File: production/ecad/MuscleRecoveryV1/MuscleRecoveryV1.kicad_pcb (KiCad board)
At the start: 4 copper layers, 115.2 x 70.5 mm, 130 parts, among them IC1 LC709203FQH-01TWG, J1 AudioJack3, J2 Screw_Terminal_01x03, J3 Motor_Screw_Terminal, J4 USB_C_Receptacle_USB2.0, J5 Screw_Terminal_01x10, J6 Screw_Terminal_01x06, J7 Conn_01x11_Pin, Q1 FDN340P, Q2 AO3400A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

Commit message: pushing current layout and other changes to be able to pull
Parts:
- removed J4: USB_C_Receptacle_USB2.0, Connector_USB:USB_C_Plug_Molex_105444
- added J8: Screw_Terminal_01x07, Connector_PinHeader_2.54mm:PinHeader_1x07_P2.54mm_Vertical, F.Cu at (117.9, 173.6)
- added J9: Screw_Terminal_01x02, Connector_PinHeader_2.54mm:PinHeader_1x02_P2.54mm_Vertical, F.Cu at (218.2, 83.4)
- J5: value Screw_Terminal_01x10 -> USB4110-GF-A; footprint Connector_PinHeader_2.54mm:PinHeader_1x10_P2.54mm_Vertical -> Muscle_Recovery_Footprint_Library:USB4110-GF-A_GCT
- R63: value 0 -> DNP
- moved R24 156.8 mm to (102.9, 165.9), turned to 90 degrees
- moved R46 155.6 mm to (107.7, 162.6)
- moved R4 154.6 mm to (99.9, 156.5)
- moved R63 154.4 mm to (113.8, 161.2), turned to 180 degrees
- moved R23 154.4 mm to (102.8, 151.1)
- moved R7 153.3 mm to (99.8, 158.8)
- moved C3 152.8 mm to (99.7, 162.6), turned to 180 degrees
- moved R45 152.5 mm to (108.0, 144.0)
- moved R22 151.0 mm to (106.8, 151.1)
- moved R6 150.9 mm to (103.7, 162.6), turned to 180 degrees
- moved R5 150.3 mm to (103.7, 156.5)
- moved R64 149.9 mm to (117.7, 161.2)
- moved R28 149.7 mm to (117.7, 164.0)
- moved R19 149.6 mm to (110.1, 150.4), turned to 90 degrees
- moved C4 146.6 mm to (104.4, 159.5), turned to 90 degrees
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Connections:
- C16 pad 1: +3.3V -> +3V3
- C8 pad 1: +3.3V -> +3V3
- C9 pad 1: +3.3V -> +3V3
- D7 pad 1: +3.3V -> +3V3
- J1 pad 1: (no net) -> RA
- J1 pad 2: (no net) -> RL
- J1 pad 3: (no net) -> LA
- J3 pad 1: +3.3V -> +3V3
- J6 pad 2: IO35 -> IO17
- J7 pad 2: +3.3V -> +3V3
- R10 pad 1: Net-(J4-CC1) -> Net-(J5-CC1)
- R11 pad 1: +3.3V -> +3V3
- R12 pad 1: +3.3V -> +3V3
- R16 pad 1: +3.3V -> +3V3
- R36 pad 1: +BATT -> +3V3
- R9 pad 1: Net-(J4-CC2) -> Net-(J5-CC2)
- S1 pad 4: +3.3V -> +3V3
- S4 pad 4: +3.3V -> +3V3
- SCL1 pad 1: SDA -> SCL
- TFT_CLK1 pad 1: TFT_CLK -> SCK
- U1 pad 2: +3.3V -> +3V3
- U3 pad 6: +3.3V -> +3V3
- U3 pad 7: +3.3V -> +3V3
- U6 pad 28: unconnected-(U6-IO17-Pad28) -> IO17
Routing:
- net IO26: track 0.00 -> 19.6 mm
- net IO27: track 0.00 -> 14.7 mm
- net IO32: track 0.00 -> 13.7 mm
- added copper zone on In1.Cu, net GND

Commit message: saving changes
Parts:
- moved J8 62.9 mm to (118.1, 110.8), turned to 0 degrees
- moved R24 60.7 mm to (125.2, 109.5), turned to 0 degrees
- moved C3 60.6 mm to (128.8, 109.5), turned to 0 degrees
- moved R7 59.4 mm to (131.8, 108.8), turned to -90 degrees
- moved R4 59.0 mm to (134.8, 108.9), turned to -90 degrees
- moved IO0 57.9 mm to (176.3, 109.8)
- moved TP4 56.8 mm to (178.3, 127.9)
- moved R6 56.4 mm to (128.8, 112.1), turned to 0 degrees
- moved D5 55.8 mm to (123.2, 112.7)
- moved R23 55.1 mm to (138.4, 109.0), turned to -90 degrees
- moved C4 54.2 mm to (131.8, 112.7)
- moved R5 53.8 mm to (134.8, 112.6), turned to -90 degrees
- moved R46 52.6 mm to (128.8, 114.5), turned to 180 degrees
- moved R62 50.8 mm to (152.3, 101.3), turned to -90 degrees
- moved C10 50.8 mm to (141.9, 111.9)
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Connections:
- J6 pad 2: IO17 -> IO32
- J6 pad 3: IO32 -> IO17
- J6 pad 4: IO27 -> IO26
- J6 pad 5: IO26 -> IO27
- J8 pad 3: LOD+ -> LOD-
- J8 pad 4: LOD- -> LOD+
- J8 pad 5: REF -> SDN
- J8 pad 7: SDN -> REF
- R44 pad 1: Net-(U5-FR) -> SW
- R44 pad 2: SW -> Net-(U5-FR)
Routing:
- net IO26: track 19.6 -> 0.00 mm
- net IO27: track 14.7 -> 0.00 mm
- net IO32: track 13.7 -> 0.00 mm
- net +3V3: track 6.19 -> 0.00 mm
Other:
- board size 115.2 x 70.5 mm -> 92.6 x 67.3 mm

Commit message: my first complete pcb draft
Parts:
- moved GND1 17.0 mm to (162.5, 129.2)
- moved 3v31 14.0 mm to (166.5, 129.2)
- moved SCL1 9.33 mm to (178.8, 81.9)
- moved SDA1 3.45 mm to (177.7, 75.1)
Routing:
- net GND: track 0.00 -> 101.9 mm, vias 0 -> 43
- net SDA: track 0.00 -> 99.5 mm, vias 0 -> 2
- net SCK: track 0.00 -> 91.6 mm, vias 0 -> 2
- net +3V3: track 0.00 -> 88.5 mm, vias 0 -> 25
- net EN: track 0.00 -> 86.1 mm, vias 0 -> 2
- net TFT_RST: track 0.00 -> 77.8 mm, vias 0 -> 2
- net MISO: track 0.00 -> 76.4 mm, vias 0 -> 2
- net SCL: track 0.00 -> 68.8 mm
- net MOSI: track 0.00 -> 66.8 mm, vias 0 -> 2
- net REF: track 0.00 -> 63.5 mm, vias 0 -> 2
- net IO0: track 0.00 -> 56.1 mm
- net LIT: track 0.00 -> 54.4 mm
- net TFT_DC: track 0.00 -> 53.0 mm, vias 0 -> 2
- net RXD0: track 0.00 -> 49.9 mm, vias 0 -> 2
- net Vout: track 0.00 -> 49.9 mm
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- added copper zone on In2.Cu, net +3V3
- added copper zone on In2.Cu, net +BATT
- added copper zone on In2.Cu, net VBUS

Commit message: final pcb updates
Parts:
- moved C8 12.9 mm to (193.3, 111.9), turned to 90 degrees
- moved C17 11.9 mm to (203.2, 83.1), turned to 90 degrees
- moved C9 10.8 mm to (195.5, 111.9), turned to 90 degrees
- moved SDA1 8.44 mm to (185.5, 78.3)
- moved SCL1 7.97 mm to (176.9, 74.2)
- moved D2 3.89 mm to (186.6, 99.6), turned to 0 degrees
- moved C15 2.67 mm to (186.1, 97.2), turned to 0 degrees
- moved R31 2.22 mm to (177.9, 76.7), turned to 0 degrees
- moved C5 2.19 mm to (204.1, 98.0), turned to 0 degrees
- moved R30 2.08 mm to (177.9, 79.5)
- moved TFT_CLK1 1.68 mm to (127.6, 102.9)
- moved R51 1.34 mm to (121.7, 94.4)
- moved R50 1.29 mm to (121.7, 97.2)
- moved R52 1.28 mm to (121.7, 91.6)
- moved R56 1.26 mm to (121.7, 81.0)
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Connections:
- C17 pad 1: +BATT -> GND
- C17 pad 2: GND -> +BATT
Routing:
- net SDA: track 99.5 -> 78.7 mm
- net IO0: track 56.1 -> 38.7 mm, vias 0 -> 2
- net GND: track 101.9 -> 88.7 mm, vias 43 -> 40
- net RTS: track 21.4 -> 10.1 mm
- net USB-: track 10.4 -> 20.6 mm, vias 0 -> 2
- net SCL: track 68.8 -> 78.9 mm, vias 0 -> 2
- net USB+: track 13.3 -> 20.6 mm
- net +3V3: track 88.5 -> 82.8 mm, vias 25 -> 24
- net VBUS: track 30.9 -> 25.8 mm
- net +BATT: track 21.9 -> 18.0 mm, vias 4 -> 3
- net TFT_RST: track 77.8 -> 81.5 mm
- net DTR: track 23.4 -> 20.0 mm
- net Net-(D2-K): track 8.14 -> 5.03 mm
- net Net-(U3-~{RST}): track 3.44 -> 0.50 mm
- net SCK: track 91.6 -> 94.2 mm
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- added copper zone on F.Cu, net +3V3

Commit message: extra save
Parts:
- moved R15 13.4 mm to (192.3, 120.3), turned to 180 degrees
- moved R13 12.6 mm to (192.3, 113.7), turned to 0 degrees
- moved R14 12.6 mm to (192.3, 116.0), turned to 180 degrees
- moved R16 12.0 mm to (192.3, 118.3), turned to 0 degrees
- moved R17 11.6 mm to (203.6, 115.8), turned to 0 degrees
- moved R18 11.4 mm to (203.6, 117.9), turned to 0 degrees
- moved R40 4.34 mm to (185.5, 121.4), turned to 90 degrees
- moved SD_CS1 3.85 mm to (124.8, 83.8)
- moved TFT_CLK1 3.84 mm to (124.9, 100.2)
- moved TFT_DC1 3.37 mm to (124.8, 86.4)
- moved MOSI1 3.33 mm to (124.9, 94.5)
- moved TFT_CS1 3.19 mm to (124.8, 91.7)
- moved MISO1 3.08 mm to (124.9, 97.2)
- moved TFT_RST1 2.96 mm to (124.8, 89.0)
- moved R57 1.75 mm to (143.6, 83.6)
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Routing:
- net GND: track 88.7 -> 129.9 mm, vias 40 -> 45
- net DTR: track 20.0 -> 39.1 mm, vias 0 -> 2
- net TXD0: track 48.1 -> 65.8 mm
- net RXD0: track 49.9 -> 63.3 mm
- net RTS: track 10.1 -> 22.7 mm
- net VBUS: track 25.8 -> 35.7 mm, vias 5 -> 7
- net Net-(D2-K): track 5.03 -> 13.2 mm
- net +3V3: track 82.8 -> 87.4 mm, vias 24 -> 31
- net /Bootloading/DTR_Q: track 6.24 -> 3.06 mm
- net Net-(U3-~{RST}): track 0.50 -> 3.61 mm
- net /Bootloading/SUS_IN: track 1.65 -> 4.70 mm
- net Net-(U5-RLDFB): track 9.78 -> 12.5 mm
- net TFT_RST: track 81.5 -> 79.0 mm
- net SD_CS: track 36.7 -> 34.5 mm
- net +BATT: track 18.0 -> 20.1 mm, vias 3 -> 4
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
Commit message: updated bom
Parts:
- added C20: 1uF, Capacitor_SMD:C_0805_2012Metric, F.Cu at (166.7, 141.7)
- added C21: 0.1uF, Capacitor_SMD:C_0805_2012Metric, F.Cu at (166.7, 144.7)
- added R27: 0, Resistor_SMD:R_0805_2012Metric, F.Cu at (166.7, 147.6)
- added R65: 0, Resistor_SMD:R_0805_2012Metric, F.Cu at (166.7, 150.6)
- added U4: ADXL343, Package_LGA:LGA-14_3x5mm_P0.8mm_LayoutBorder1x6y, F.Cu at (162.2, 143.4)
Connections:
- C17 pad 1: GND -> +BATT
- C17 pad 2: +BATT -> GND
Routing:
- net GND: track 129.9 -> 128.4 mm, vias 45 -> 44
- net +BATT: track 20.1 -> 21.6 mm, vias 4 -> 5

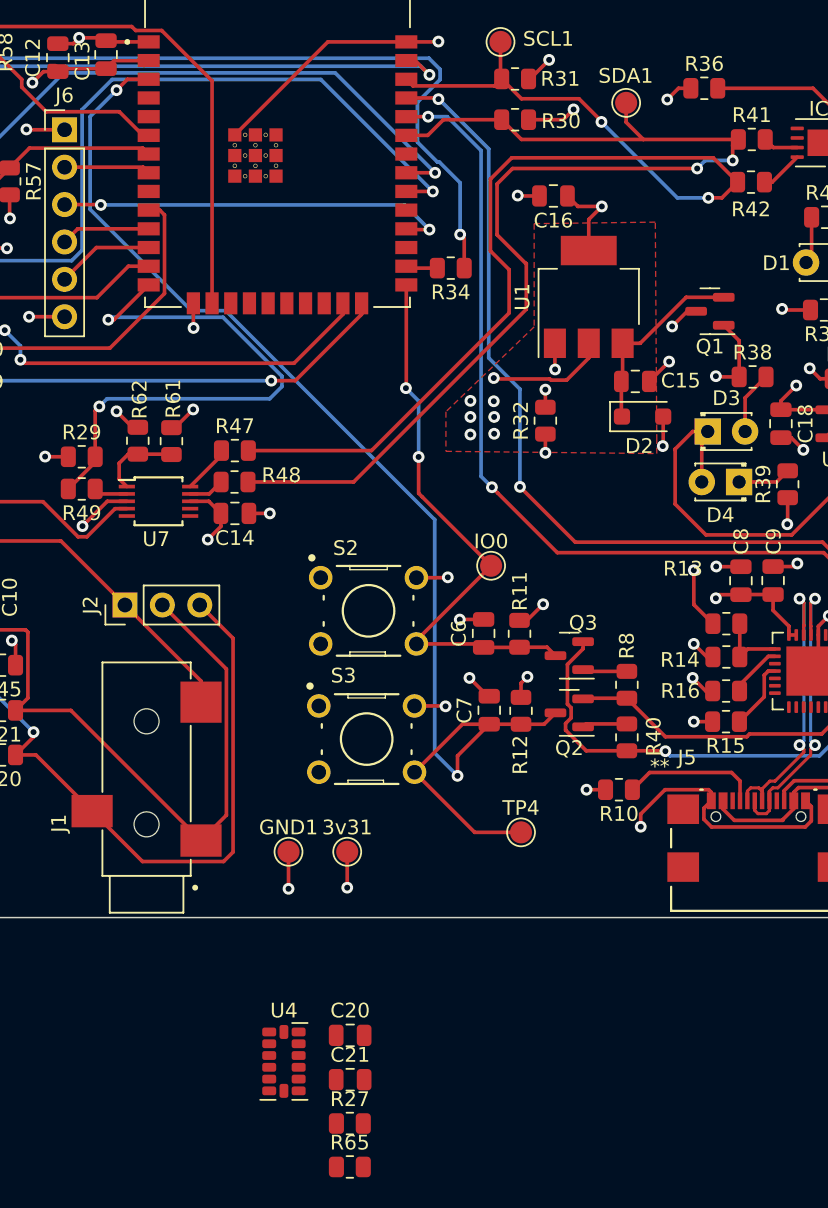
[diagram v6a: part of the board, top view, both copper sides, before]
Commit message: added accelerometer to layout
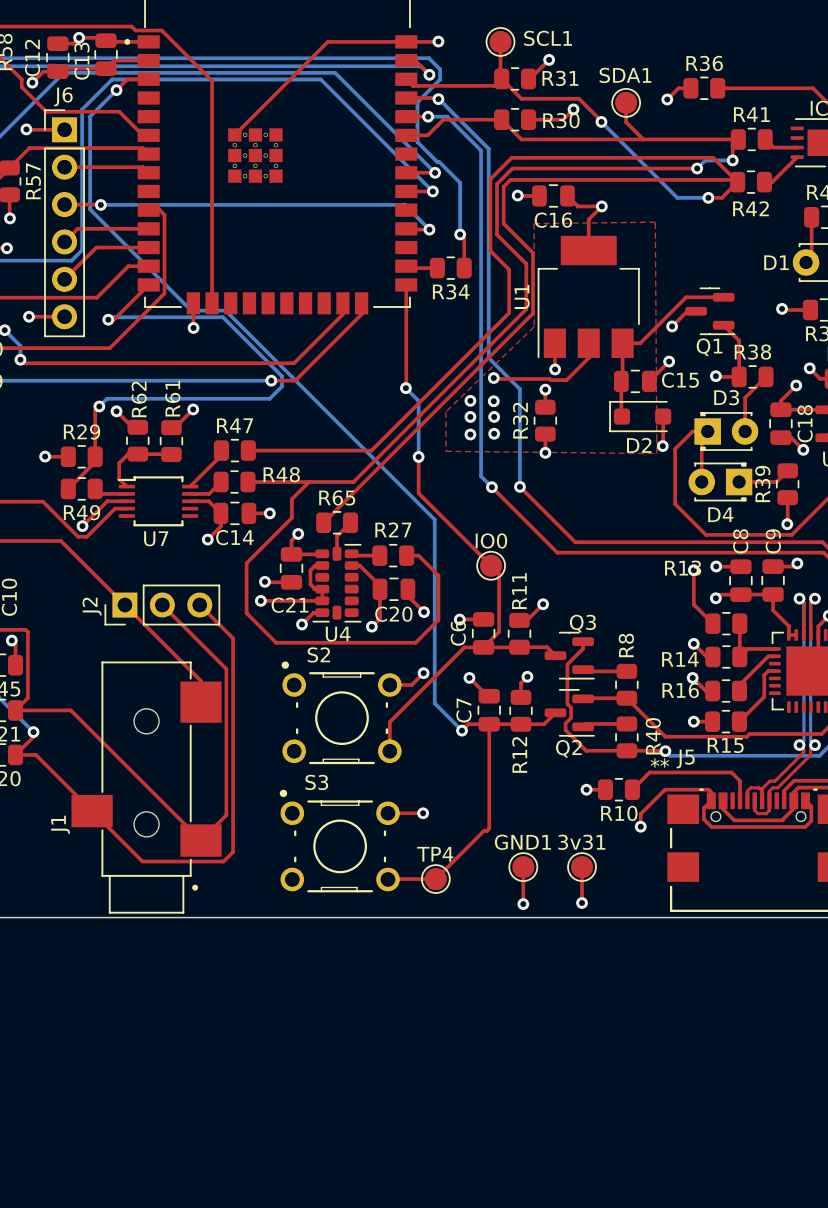
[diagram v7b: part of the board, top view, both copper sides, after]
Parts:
- moved R65 43.8 mm to (165.8, 106.8)
- moved R27 38.7 mm to (169.6, 109.1), turned to 180 degrees
- moved C21 35.0 mm to (162.7, 109.9), turned to -90 degrees
- moved U4 32.7 mm to (165.8, 110.9)
- moved C20 30.4 mm to (169.7, 111.4)
- moved 3v31 16.0 mm to (182.5, 130.2)
- moved GND1 16.0 mm to (178.5, 130.2)
- moved S2 7.51 mm to (166.2, 120.1)
- moved S3 7.51 mm to (166.0, 128.8)
- moved TP4 6.60 mm to (172.5, 131.0)
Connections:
- C17 pad 1: +BATT -> GND
- C17 pad 2: GND -> +BATT
- C20 pad 1: +3.3V -> +3V3
- C21 pad 1: +3.3V -> +3V3
- U4 pad 1: +3.3V -> +3V3
- U4 pad 12: +3.3V -> +3V3
- U4 pad 6: +3.3V -> +3V3
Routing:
- net SCL: track 78.9 -> 124.6 mm
- net SDA: track 77.9 -> 108.8 mm
- net GND: track 128.4 -> 142.8 mm, vias 44 -> 48
- net +3V3: track 87.4 -> 98.3 mm, vias 31 -> 34
- net EN: track 86.1 -> 80.8 mm
- net IO0: track 38.7 -> 43.6 mm
- net Net-(U4-SCL/SCLK): track 0.00 -> 2.49 mm
- net Net-(U4-SDA/SDI/SDIO): track 0.00 -> 1.96 mm
- net +BATT: track 21.6 -> 20.1 mm, vias 5 -> 4
